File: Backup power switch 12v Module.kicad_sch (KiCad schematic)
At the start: 23 parts, among them J1 BAT/PWR IN, K1 SRD-12VDC-SL-C, Q3 BSS138, U1 LM393

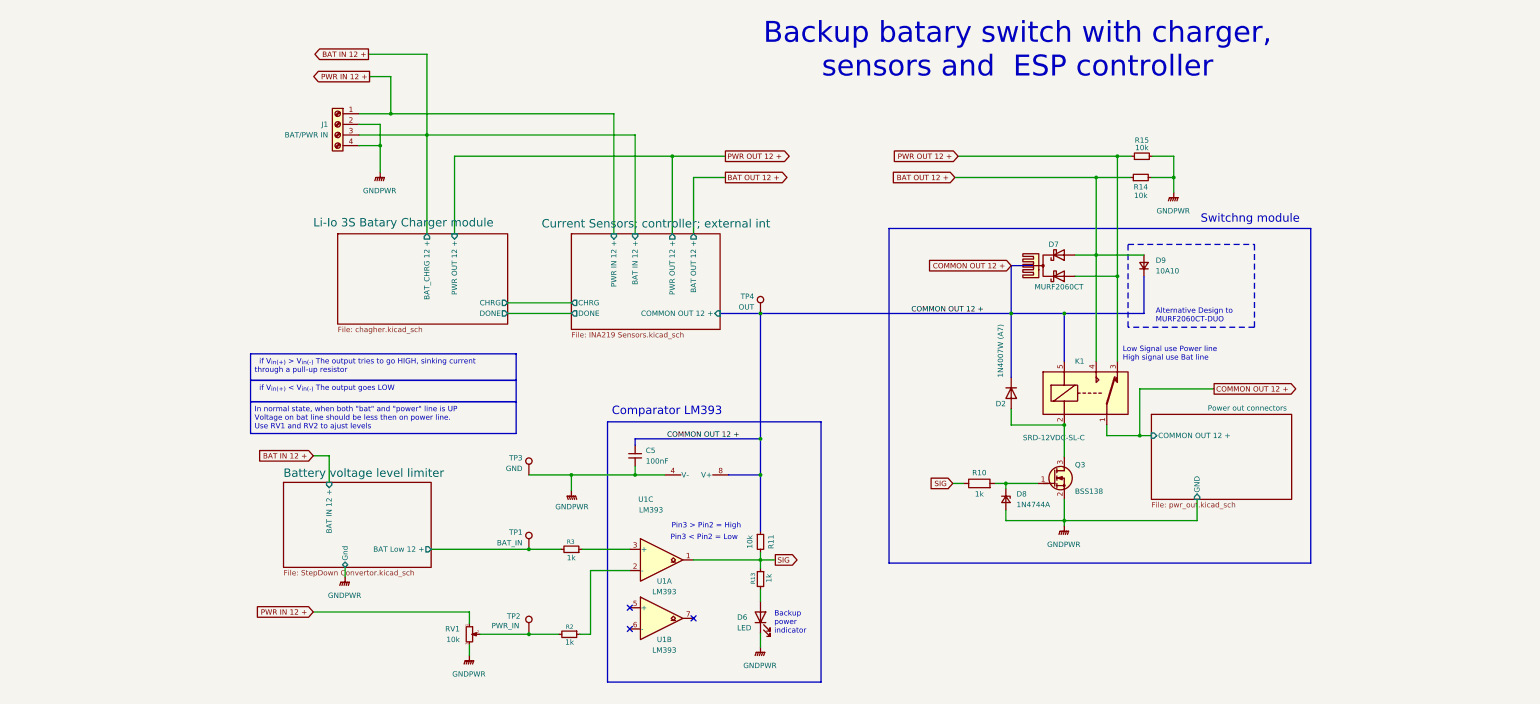
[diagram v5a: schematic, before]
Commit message: Clean space for second relay
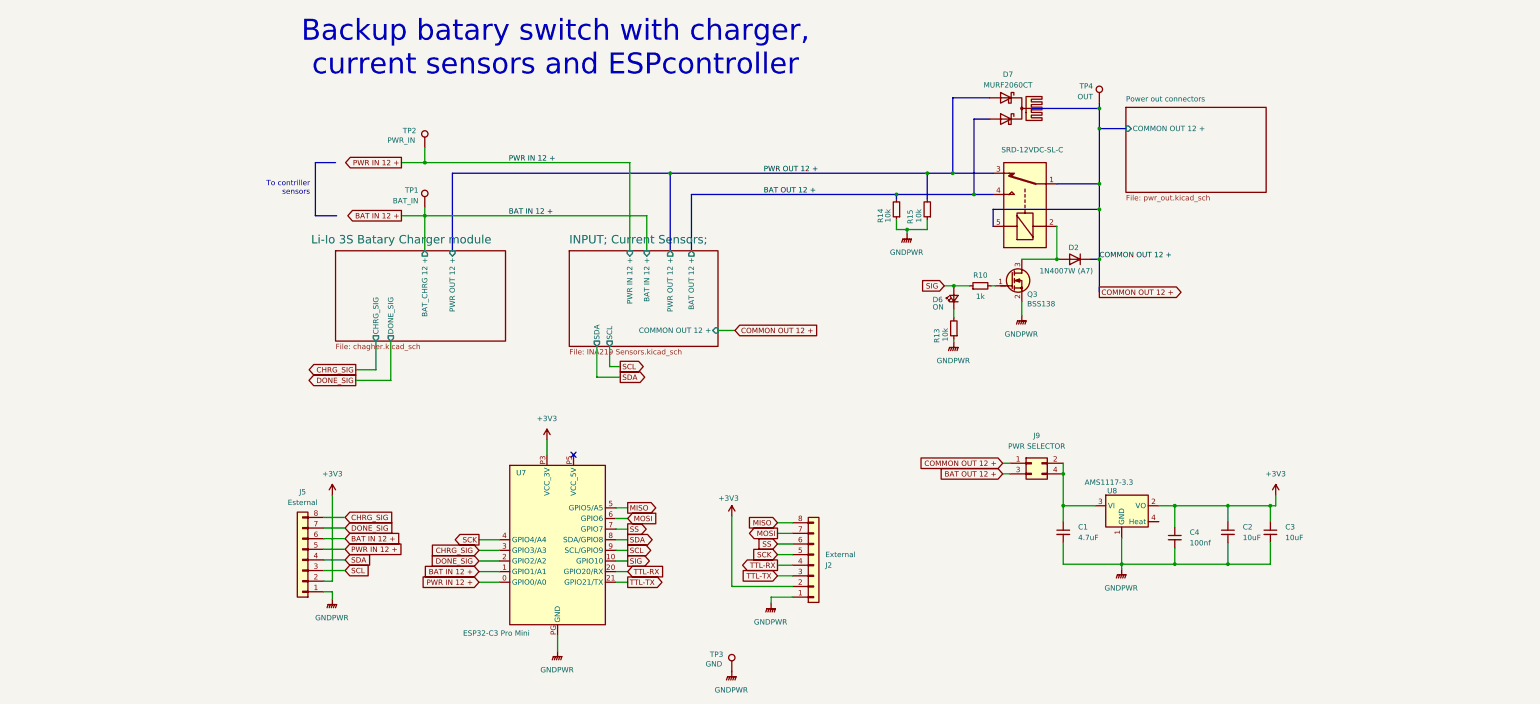
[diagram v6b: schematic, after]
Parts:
- removed C5: 100nF, Capacitor_SMD:C_0805_2012Metric_Pad1.18x1.45mm_HandSolder, symbol Device:C_Small
- removed D6: LED, LED_SMD:LED_0603_1608Metric_Pad1.05x0.95mm_HandSolder, symbol Device:LED
- removed D8: 1N4744A, Diode_THT:D_DO-41_SOD81_P7.62mm_Horizontal, symbol Device:D_Zener_Small
- removed D9: 10A10, symbol Device:D_Small
- removed J1: BAT/PWR IN, TerminalBlock_Local:ScrewTerminal_KF7.62_4P, symbol Connector:Screw_Terminal_01x04
- removed R11: 10k, Resistor_SMD:R_0805_2012Metric_Pad1.20x1.40mm_HandSolder, symbol Device:R_Small
- removed R2, R3: 1k, Resistor_SMD:R_0805_2012Metric_Pad1.20x1.40mm_HandSolder, symbol Device:R_Small
- removed RV1: 10k, PCM_Potentiometer_THT_AKL:Potentiometer_Bourns_3296W_Vertical, symbol Device:R_Potentiometer_Small
- removed U1: LM393, Package_DIP:DIP-8_W7.62mm, symbol Comparator:LM393
- added C1: 4.7uF, Capacitor_SMD:C_1210_3225Metric_Pad1.33x2.70mm_HandSolder, symbol Device:C_Small
- added C2, C3: 10uF, Capacitor_Tantalum_SMD:CP_EIA-3528-21_Kemet-B_HandSolder, symbol Device:C_Small
- added C4: 100nf, Capacitor_SMD:C_0805_2012Metric_Pad1.18x1.45mm_HandSolder, symbol Device:C_Small
- added D6: ON, LED_SMD:LED_0603_1608Metric_Pad1.05x0.95mm_HandSolder, symbol Device:LED_Small
- added J2: External, Connector_JST:JST_PH_B8B-PH-K_1x08_P2.00mm_Vertical, symbol Connector_Generic:Conn_01x08
- added J5: Esternal, Connector_JST:JST_PH_B8B-PH-K_1x08_P2.00mm_Vertical, symbol Connector_Generic:Conn_01x08
- added J9: PWR SELECTOR, Connector_PinHeader_2.54mm:PinHeader_2x02_P2.54mm_Vertical, symbol Connector_Generic:Conn_02x02_Odd_Even
- added U7: ESP32-C3 Pro Mini, WIFI_Module:ESP32-C3_Pro_mini_pin, symbol MCU_Module_local:ESP32_C3_Pro_Mini
- added U8: AMS1117-3.3, Package_TO_SOT_SMD:SOT-223-3_TabPin2, symbol Regulator_Linear:AMS1117-3.3
- R10: symbol Device:R -> Device:R_Small
- R13: value 1k -> 10k
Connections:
- net Battery voltage level limiter/BAT Low 12 + is gone; now on net BAT IN 12 +: TP1.1
- net BAT IN 12 +: now also J5.6 (Pin_6), U7.1 (GPIO1/A1)
- net BAT OUT 12 +: now also J9.3 (Pin_3); no longer D7.1 (A1), K1.4, R14.1
- net COMMON OUT 12 +: now also J9.1 (Pin_1); no longer K1.1
- net GNDPWR: now also R13.1, R14.1, R15.1, C1.2, C2.2, C3.2, C4.2, J2.1 (Pin_1), J5.1 (Pin_1), U7.PG (GND), U8.1 (GND); no longer R14.2, R15.2
- net PWR IN 12 +: now also TP2.1, J5.5 (Pin_5), U7.0 (GPIO0/A0)
- net PWR OUT 12 +: no longer D7.3 (A2), K1.3, R15.1
- net SIG: now also D6.2 (A), U7.10 (GPIO10); no longer R13.1
- net at R13.2: now also D6.1 (K)
- new net: C1.1, J9.2 (Pin_2), J9.4 (Pin_4), U8.3 (VI)
- new net +3V3: C2.1, C3.1, C4.1, J2.2 (Pin_2), J5.2 (Pin_2), U7.P3 (VCC_3V), U8.2 (VO)
- new net CHRG_SIG: J5.8 (Pin_8), U7.3 (GPIO3/A3)
- new net DONE_SIG: J5.7 (Pin_7), U7.2 (GPIO2/A2)
- new net MISO: J2.8 (Pin_8), U7.5 (GPIO5/A5)
- new net MOSI: J2.7 (Pin_7), U7.6 (GPIO6)
- new net SCK: J2.5 (Pin_5), U7.4 (GPIO4/A4)
- new net SCL: J5.3 (Pin_3), U7.9 (SCL/GPIO9)
- new net SDA: J5.4 (Pin_4), U7.8 (SDA/GPIO8)
- new net SS: J2.6 (Pin_6), U7.7 (GPIO7)
- new net TTL-RX: J2.4 (Pin_4), U7.20 (GPIO20/RX)
- new net TTL-TX: J2.3 (Pin_3), U7.21 (GPIO21/TX)
- no-connect marks 3 -> 1
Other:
- sheet Current Sensors; controller; external int renamed INPUT; Current Sensors;
- removed sheet Battery voltage level limiter
- sheet INPUT; Current Sensors; ports: added SCL, SDA; removed CHRG, DONE
- sheet Li-Io 3S Batary Charger module ports: added CHRG_SIG, DONE_SIG; removed CHRG, DONE
- sheet Power out connectors ports: added none; removed GND
- note added: "Backup batary switch with charger, current sensors and ESPcontroller"
- note added: "To contriller sensors"
- note removed: "Alternative Design to MURF2060CT-DUO"
- note removed: "Backup batary switch with charger, sensors and ESP controller"
- note removed: "Backup power indicator"
- note removed: "Comparator LM393"
- note removed: "Low Signal use Power line High signal use Bat line"
- note removed: "Pin3 < Pin2 = Low"
- note removed: "Pin3 > Pin2 = High"
- note removed: "Switchng module"
- moved on the sheet: D2, D7, Q3, R10, R14, R15, TP1, TP2, TP4

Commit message: Place second relay
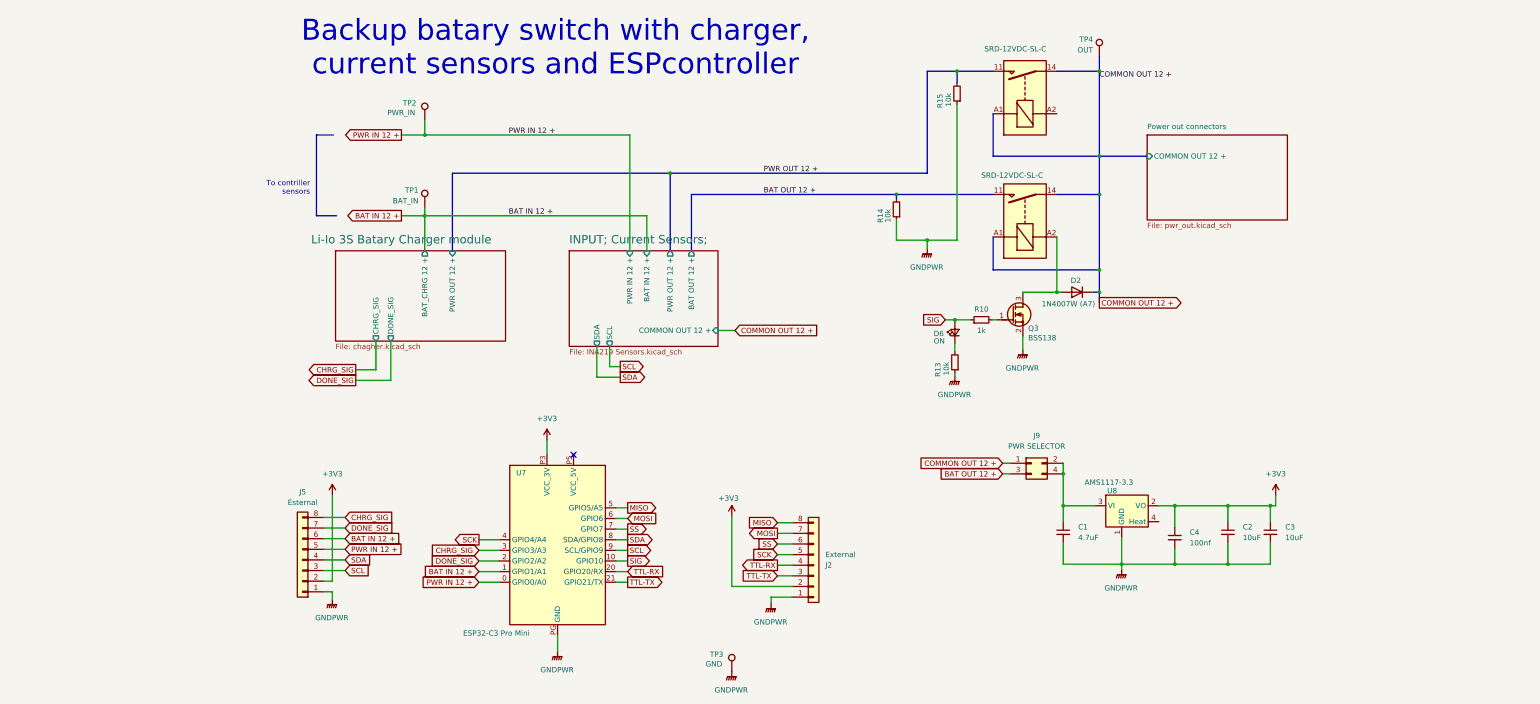
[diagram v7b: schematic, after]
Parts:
- removed D7: MURF2060CT, PCM_Package_TO_SOT_THT_AKL_OneLayer:TO-220-3_Staggered_Vertical, symbol Diode:C3D20065D
- removed HS1: Heatsink, Heatsink:Heatsink_Stonecold_HS-S01_13.21x6.35mm, symbol Mechanical:Heatsink
- added K2: SRD-12VDC-SL-C, Relay_THT:Relay_SPST_Schrack-RP-II-1-FormA_RM3.5mm, symbol Relay_Local:SMIH-S-112LM
- K1: footprint Relay_THT:Relay_SPDT_SANYOU_SRD_Series_Form_C -> Relay_THT:Relay_SPST_Schrack-RP-II-1-FormA_RM3.5mm; symbol Relay_Local:SANYOU_SRD_Form_C -> Relay_Local:SMIH-S-112LM
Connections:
- net at D2.2 (A), Q3.3 (D): now also K1.A2; no longer K1.2
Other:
- moved on the sheet: D2, D6, Q3, R10, R13, R15, TP2, TP4

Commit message: Connect srcond relay
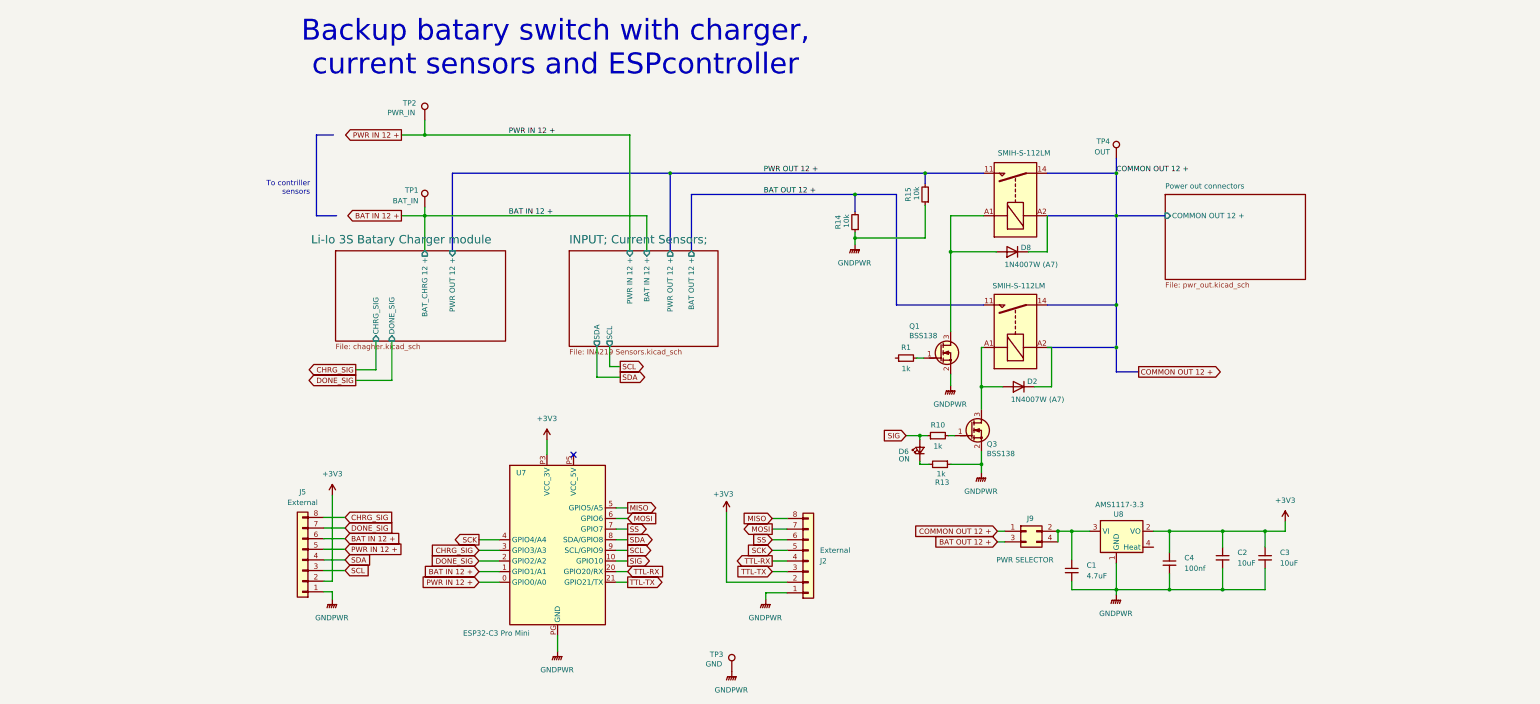
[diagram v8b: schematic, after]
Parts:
- added D8: 1N4007W (A7), Diode_SMD:D_SOD-123F, symbol Device:D
- added Q1: BSS138, PCM_Package_TO_SOT_SMD_AKL:SOT-23, symbol PCM_Transistor_MOSFET_AKL:BSS138
- added R1: 1k, Resistor_SMD:R_0805_2012Metric_Pad1.20x1.40mm_HandSolder, symbol Device:R_Small
- J5: value Esternal -> External
- K1, K2: value SRD-12VDC-SL-C -> SMIH-S-112LM
- R13: value 10k -> 1k
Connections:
- net GNDPWR: now also Q1.2 (S)
- net at D2.1 (K): now also K1.A2
- net at D2.2 (A), Q3.3 (D): now also K1.A1; no longer K1.A2
- net at K2.A1: now also D8.2 (A), Q1.3 (D)
- net at K2.A2: now also D8.1 (K)
- new net: Q1.1 (G), R1.2
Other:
- sheet INPUT; Current Sensors; ports: added none; removed COMMON OUT 12 +
- moved on the sheet: C1, C2, C3, C4, D2, D6, J2, J9, Q3, R10, R13, R14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
